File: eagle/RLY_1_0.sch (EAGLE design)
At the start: 27 parts, among them K1 G5V1, K2 G5V1, K3 G5V1, K4 G5V1, Q1 BC548B, Q2 BC548B, Q3 BC548B, Q4 BC548B, X1 In A

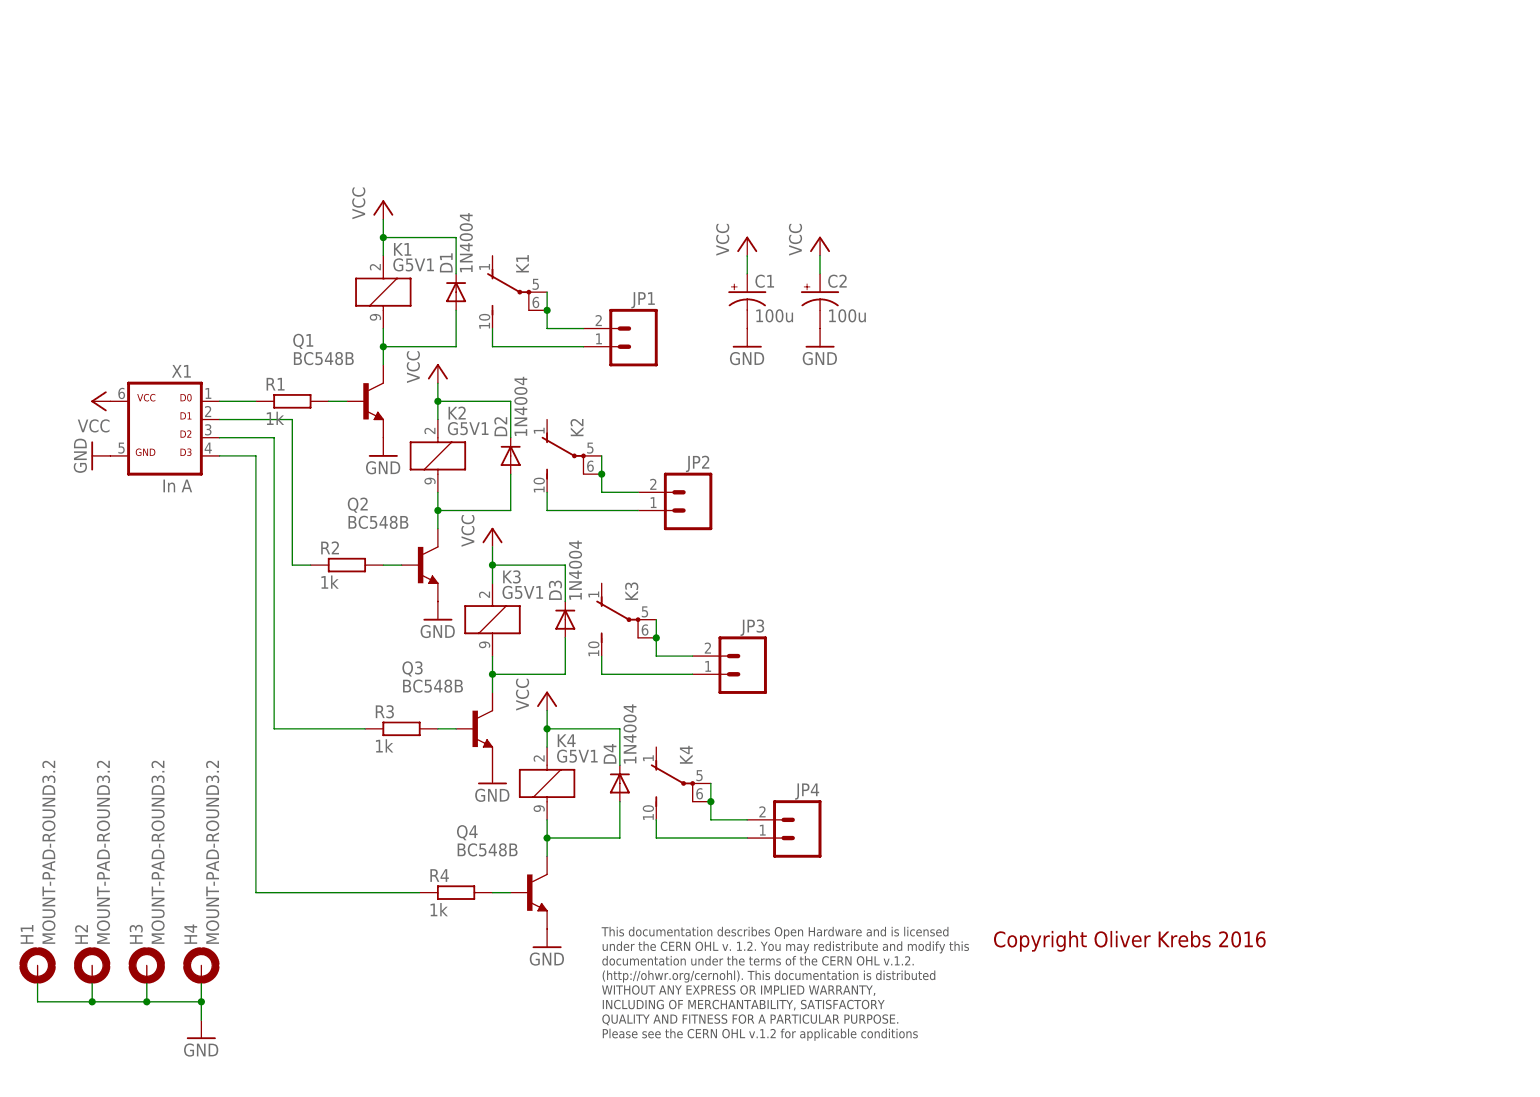
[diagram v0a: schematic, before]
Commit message: Add new tetra-Board and arduino files
Add AMP_1_0, AVC_1_0, D18_1_1, IOP_1_2, MIC_1_0, PIN_1_1, POT_1_0, PWA_1_0, PWR_1_0, RGF 2.0, SOC_2_0, VLT_1_0
Add mex_nano_shield_keyboard, mex_nano_shied_numbers

New arduino projects
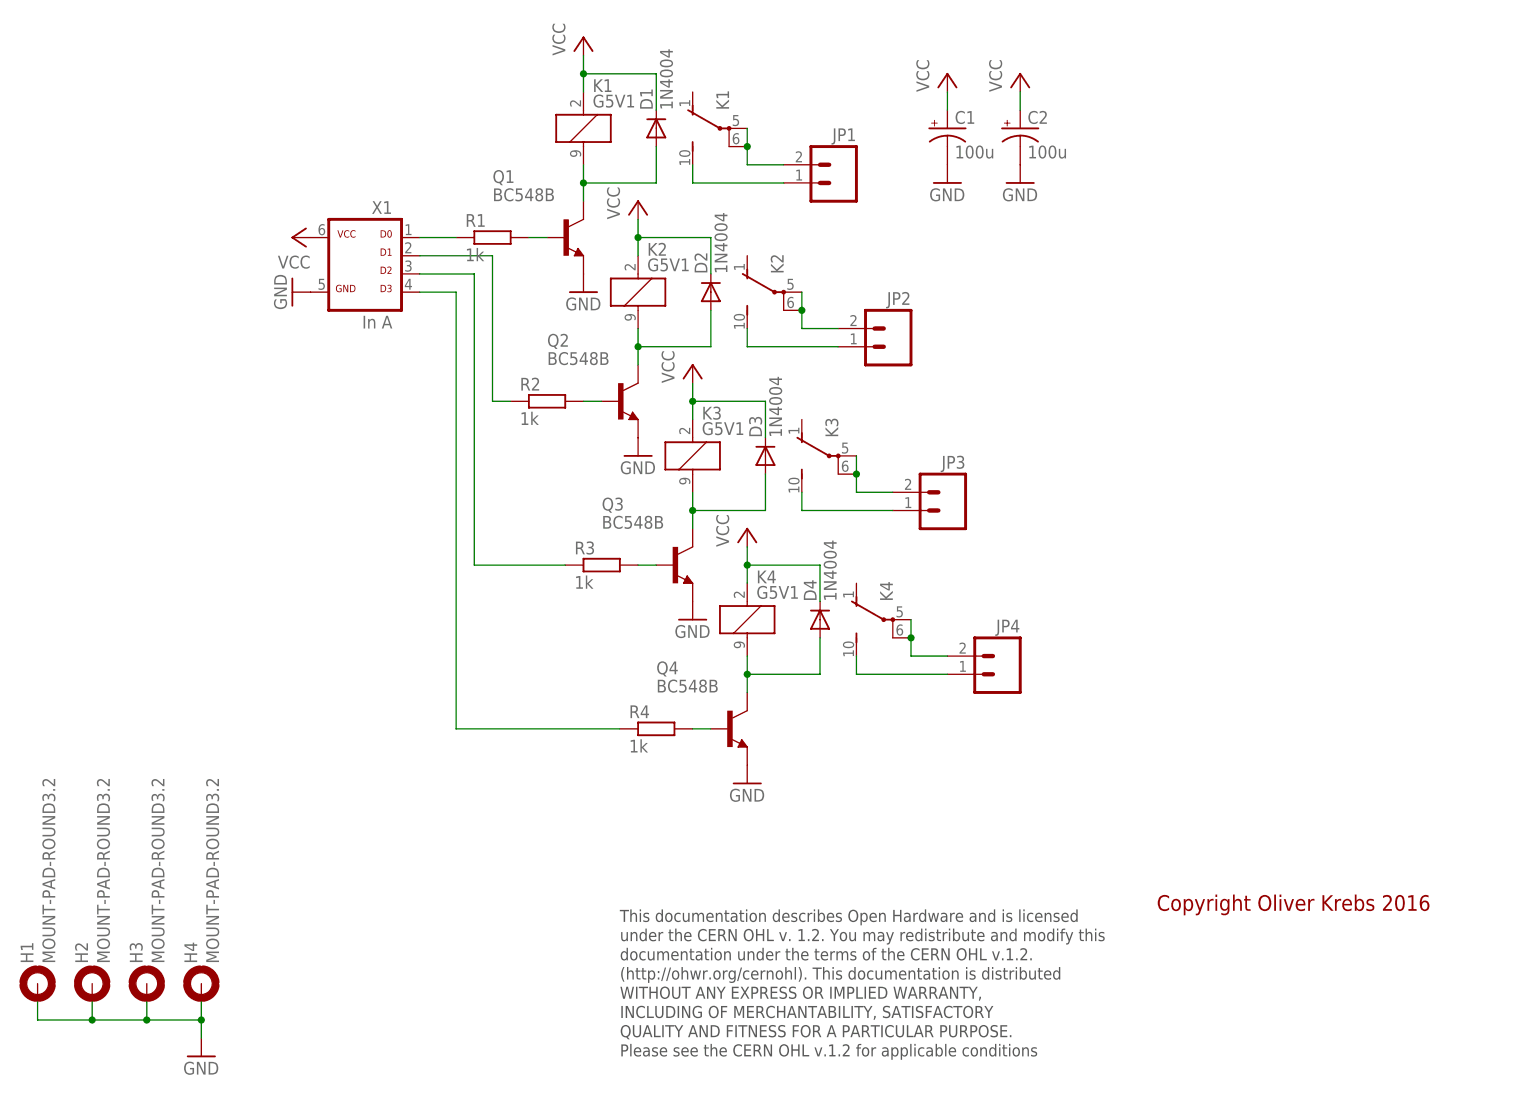
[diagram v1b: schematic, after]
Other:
- moved on the sheet: C1, C2, D1, D2, D3, D4, H1, H2, H3, H4, JP1, JP2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
